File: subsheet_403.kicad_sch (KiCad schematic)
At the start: 7 parts, among them Q405 MMBT3904

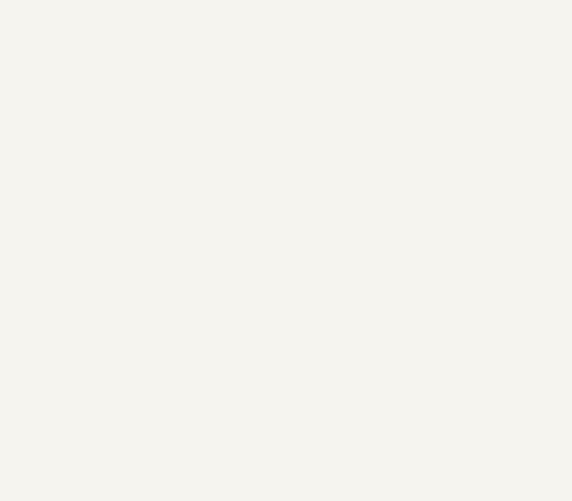
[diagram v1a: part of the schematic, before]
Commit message: add gnd/vcc symbol to start replacing local labels
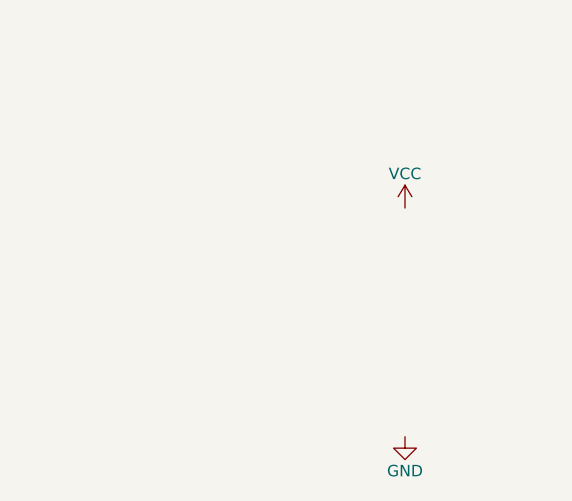
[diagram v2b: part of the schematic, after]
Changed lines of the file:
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@@
     (pin "2")
   )
+  (symbol (lib_id "power:GND") (at 181.61 234.95 0) (unit 1)
+    (in_bom yes) (on_board yes)
+    (property "Reference" "#PWR?" (id 0) (at 181.61 241.3 0)
+      (effects (font (size 1.27 1.27)) hide)
+    )
+    (property "Value" "GND" (id 1) (at 181.61 238.76 0))
+    (property "Footprint" "" (id 2) (at 181.61 234.95 0)
+      (effects (font (size 1.27 1.27)) hide)
+    )
+    (property "Datasheet" "" (id 3) (at 181.61 234.95 0)
+      (effects (font (size 1.27 1.27)) hide)
+    )
+    (pin "1")
+  )
+  (symbol (lib_id "power:VCC") (at 181.61 209.55 0) (unit 1)
+    (in_bom yes) (on_board yes)
+    (property "Reference" "#PWR?" (id 0) (at 181.61 213.36 0)
+      (effects (font (size 1.27 1.27)) hide)
+    )
+    (property "Value" "VCC" (id 1) (at 181.61 205.74 0))
+    (property "Footprint" "" (id 2) (at 181.61 209.55 0)
+      (effects (font (size 1.27 1.27)) hide)
+    )
+    (property "Datasheet" "" (id 3) (at 181.61 209.55 0)
+      (effects (font (size 1.27 1.27)) hide)
+    )
+    (pin "1")
+  )
 )
